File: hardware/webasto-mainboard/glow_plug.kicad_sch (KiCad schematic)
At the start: 23 parts, among them Q11 SSM3J374R, Q12 2N7002, Q13 SUD50P04-08, Q14 SUD50P04-08, Q15 SUD50P04-08, Q16 SUD50P04-08, Q17 SUD50P04-08, Q18 2N7002, Q19 2N7002, U6 LM7805_TO220, U7 INA219BxDCN

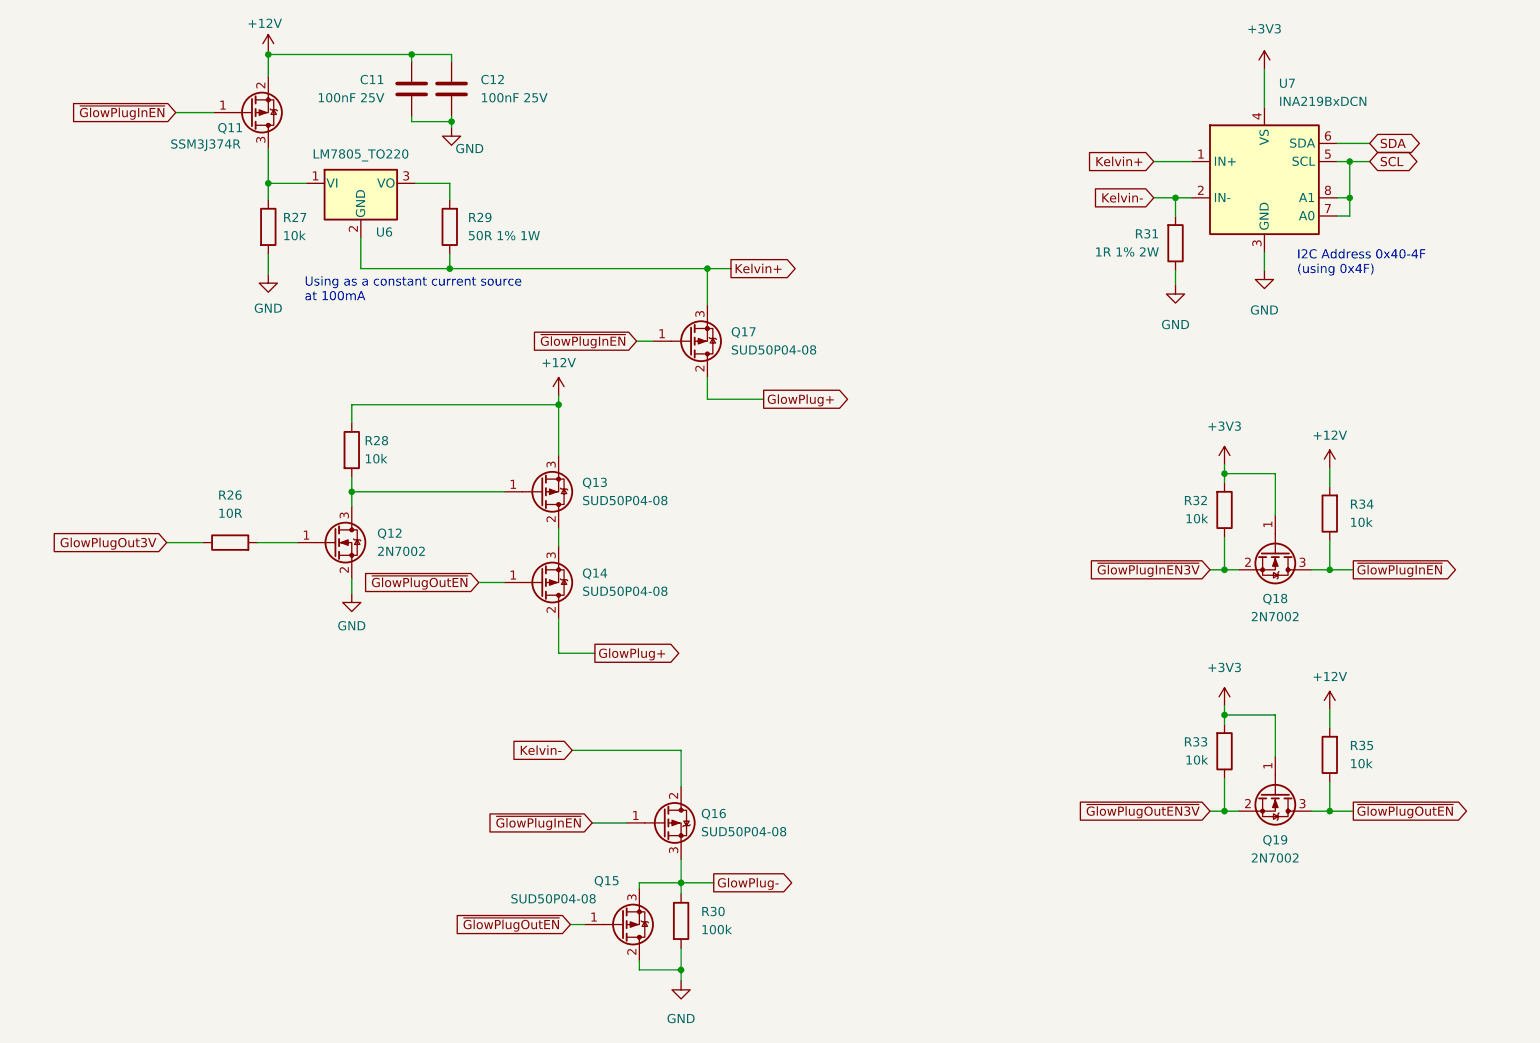
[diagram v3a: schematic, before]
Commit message: Added "USE_USB" input to choose console
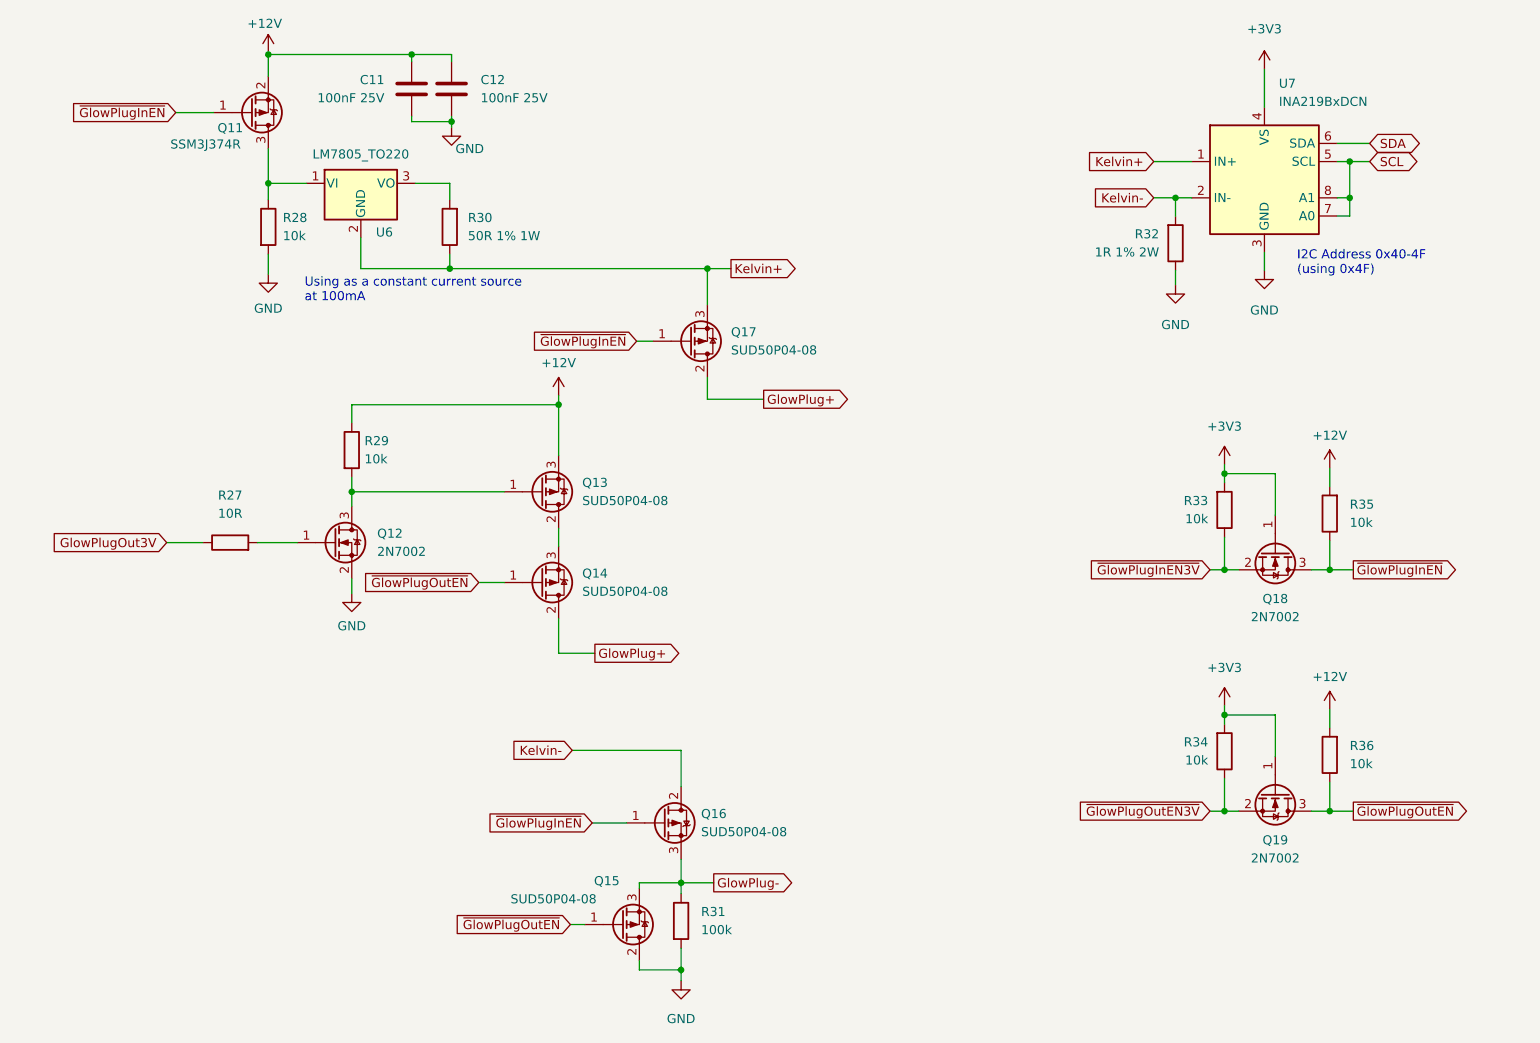
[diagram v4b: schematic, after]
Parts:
- renumbered R26 to R27, R27 to R28, R28 to R29, R29 to R30, R30 to R31, R31 to R32, R32 to R33, R33 to R34, R34 to R35, R35 to R36
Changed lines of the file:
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@@
   (symbol (lib_name "+3V3_1") (lib_id "power:+3V3") (at 202.565 29.972 0) (unit 1)
     (in_bom yes) (on_board yes) (fields_autoplaced)
-    (property "Reference" "#PWR066" (id 0) (at 202.565 33.782 0)
+    (property "Reference" "#PWR068" (id 0) (at 202.565 33.782 0)
       (effects (font (size 1.27 1.27)) hide)
     )
@@
   (symbol (lib_name "GND_8") (lib_id "power:GND") (at 202.565 58.166 0) (unit 1)
     (in_bom yes) (on_board yes) (fields_autoplaced)
-    (property "Reference" "#PWR067" (id 0) (at 202.565 64.516 0)
+    (property "Reference" "#PWR069" (id 0) (at 202.565 64.516 0)
       (effects (font (size 1.27 1.27)) hide)
     )
@@
   (symbol (lib_id "Device:R") (at 120.904 149.225 0) (unit 1)
     (in_bom yes) (on_board yes) (fields_autoplaced)
-    (property "Reference" "R30" (id 0) (at 123.698 147.9549 0)
+    (property "Reference" "R31" (id 0) (at 123.698 147.9549 0)
       (effects (font (size 1.27 1.27)) (justify left))
     )
@@
   (symbol (lib_id "Device:R") (at 74.803 83.312 0) (unit 1)
     (in_bom yes) (on_board yes) (fields_autoplaced)
-    (property "Reference" "R28" (id 0) (at 76.581 82.0419 0)
+    (property "Reference" "R29" (id 0) (at 76.581 82.0419 0)
       (effects (font (size 1.27 1.27)) (justify left))
     )
@@
   (symbol (lib_id "Device:R") (at 88.519 52.07 180) (unit 1)
     (in_bom yes) (on_board yes)
-    (property "Reference" "R29" (id 0) (at 91.059 50.7999 0)
+    (property "Reference" "R30" (id 0) (at 91.059 50.7999 0)
       (effects (font (size 1.27 1.27)) (justify right))
     )
@@
   (symbol (lib_name "+3V3_2") (lib_id "power:+3V3") (at 196.977 85.344 0) (unit 1)
     (in_bom yes) (on_board yes) (fields_autoplaced)
-    (property "Reference" "#PWR064" (id 0) (at 196.977 89.154 0)
+    (property "Reference" "#PWR066" (id 0) (at 196.977 89.154 0)
       (effects (font (size 1.27 1.27)) hide)
     )
@@
   (symbol (lib_name "GND_2") (lib_id "power:GND") (at 74.803 103.378 0) (unit 1)
     (in_bom yes) (on_board yes) (fields_autoplaced)
-    (property "Reference" "#PWR059" (id 0) (at 74.803 109.728 0)
+    (property "Reference" "#PWR061" (id 0) (at 74.803 109.728 0)
       (effects (font (size 1.27 1.27)) hide)
     )
@@
   (symbol (lib_id "Device:R") (at 63.119 52.07 0) (unit 1)
     (in_bom yes) (on_board yes)
-    (property "Reference" "R27" (id 0) (at 65.151 50.7999 0)
+    (property "Reference" "R28" (id 0) (at 65.151 50.7999 0)
       (effects (font (size 1.27 1.27)) (justify left))
     )
@@
   (symbol (lib_name "+3V3_2") (lib_id "power:+3V3") (at 196.977 119.126 0) (unit 1)
     (in_bom yes) (on_board yes) (fields_autoplaced)
-    (property "Reference" "#PWR065" (id 0) (at 196.977 122.936 0)
+    (property "Reference" "#PWR067" (id 0) (at 196.977 122.936 0)
       (effects (font (size 1.27 1.27)) hide)
     )
@@
   (symbol (lib_id "Device:R") (at 57.785 96.266 90) (unit 1)
     (in_bom yes) (on_board yes) (fields_autoplaced)
-    (property "Reference" "R26" (id 0) (at 57.785 89.662 90))
+    (property "Reference" "R27" (id 0) (at 57.785 89.662 90))
     (property "Value" "10R" (id 1) (at 57.785 92.202 90))
     (property "Footprint" "Resistor_SMD:R_0805_2012Metric_Pad1.20x1.40mm_HandSolder" (id 2) (at 57.785 98.044 90)
@@
   (symbol (lib_id "Device:R") (at 196.977 125.476 0) (mirror x) (unit 1)
     (in_bom yes) (on_board yes) (fields_autoplaced)
-    (property "Reference" "R33" (id 0) (at 194.691 124.2059 0)
+    (property "Reference" "R34" (id 0) (at 194.691 124.2059 0)
       (effects (font (size 1.27 1.27)) (justify right))
     )
@@
   (symbol (lib_name "GND_9") (lib_id "power:GND") (at 120.904 157.607 0) (unit 1)
     (in_bom yes) (on_board yes) (fields_autoplaced)
-    (property "Reference" "#PWR062" (id 0) (at 120.904 163.957 0)
+    (property "Reference" "#PWR064" (id 0) (at 120.904 163.957 0)
       (effects (font (size 1.27 1.27)) hide)
     )
@@
   (symbol (lib_name "+12V_3") (lib_id "power:+12V") (at 211.709 85.852 0) (unit 1)
     (in_bom yes) (on_board yes) (fields_autoplaced)
-    (property "Reference" "#PWR068" (id 0) (at 211.709 89.662 0)
+    (property "Reference" "#PWR070" (id 0) (at 211.709 89.662 0)
       (effects (font (size 1.27 1.27)) hide)
     )
@@
   (symbol (lib_name "GND_5") (lib_id "power:GND") (at 88.773 38.1 0) (unit 1)
     (in_bom yes) (on_board yes)
-    (property "Reference" "#PWR060" (id 0) (at 88.773 44.45 0)
+    (property "Reference" "#PWR062" (id 0) (at 88.773 44.45 0)
       (effects (font (size 1.27 1.27)) hide)
     )
@@
   (symbol (lib_id "Device:R") (at 211.709 92.202 180) (unit 1)
     (in_bom yes) (on_board yes) (fields_autoplaced)
-    (property "Reference" "R34" (id 0) (at 214.503 90.9319 0)
+    (property "Reference" "R35" (id 0) (at 214.503 90.9319 0)
       (effects (font (size 1.27 1.27)) (justify right))
     )
@@
   (symbol (lib_name "GND_8") (lib_id "power:GND") (at 190.119 60.198 0) (unit 1)
     (in_bom yes) (on_board yes) (fields_autoplaced)
-    (property "Reference" "#PWR063" (id 0) (at 190.119 66.548 0)
+    (property "Reference" "#PWR065" (id 0) (at 190.119 66.548 0)
       (effects (font (size 1.27 1.27)) hide)
     )
@@
   (symbol (lib_name "+12V_2") (lib_id "power:+12V") (at 63.119 27.686 0) (unit 1)
     (in_bom yes) (on_board yes)
-    (property "Reference" "#PWR057" (id 0) (at 63.119 31.496 0)
+    (property "Reference" "#PWR059" (id 0) (at 63.119 31.496 0)
       (effects (font (size 1.27 1.27)) hide)
     )
@@
   (symbol (lib_name "+12V_3") (lib_id "power:+12V") (at 211.709 119.634 0) (unit 1)
     (in_bom yes) (on_board yes) (fields_autoplaced)
-    (property "Reference" "#PWR069" (id 0) (at 211.709 123.444 0)
+    (property "Reference" "#PWR071" (id 0) (at 211.709 123.444 0)
       (effects (font (size 1.27 1.27)) hide)
     )
@@
   (symbol (lib_name "GND_3") (lib_id "power:GND") (at 63.119 58.674 0) (unit 1)
     (in_bom yes) (on_board yes) (fields_autoplaced)
-    (property "Reference" "#PWR058" (id 0) (at 63.119 65.024 0)
+    (property "Reference" "#PWR060" (id 0) (at 63.119 65.024 0)
       (effects (font (size 1.27 1.27)) hide)
     )
@@
   (symbol (lib_id "Device:R") (at 211.709 125.984 180) (unit 1)
     (in_bom yes) (on_board yes) (fields_autoplaced)
-    (property "Reference" "R35" (id 0) (at 214.503 124.7139 0)
+    (property "Reference" "R36" (id 0) (at 214.503 124.7139 0)
       (effects (font (size 1.27 1.27)) (justify right))
     )
@@
   (symbol (lib_id "Device:R") (at 190.119 54.356 0) (mirror x) (unit 1)
     (in_bom yes) (on_board yes) (fields_autoplaced)
-    (property "Reference" "R31" (id 0) (at 187.833 53.0859 0)
+    (property "Reference" "R32" (id 0) (at 187.833 53.0859 0)
       (effects (font (size 1.27 1.27)) (justify right))
     )
@@
   (symbol (lib_name "+12V_1") (lib_id "power:+12V") (at 103.759 75.692 0) (unit 1)
     (in_bom yes) (on_board yes) (fields_autoplaced)
-    (property "Reference" "#PWR061" (id 0) (at 103.759 79.502 0)
+    (property "Reference" "#PWR063" (id 0) (at 103.759 79.502 0)
       (effects (font (size 1.27 1.27)) hide)
     )
@@
   (symbol (lib_id "Device:R") (at 196.977 91.694 0) (mirror x) (unit 1)
     (in_bom yes) (on_board yes) (fields_autoplaced)
-    (property "Reference" "R32" (id 0) (at 194.691 90.4239 0)
-      (effects (font (size 1.27 1.27)) (justify right))
-    )
+    (property "Reference" "R33" (id 0) (at 194.691 90.4239 0)
+      (effects (font (size 1.27 1.27)) (justify right))
+    )

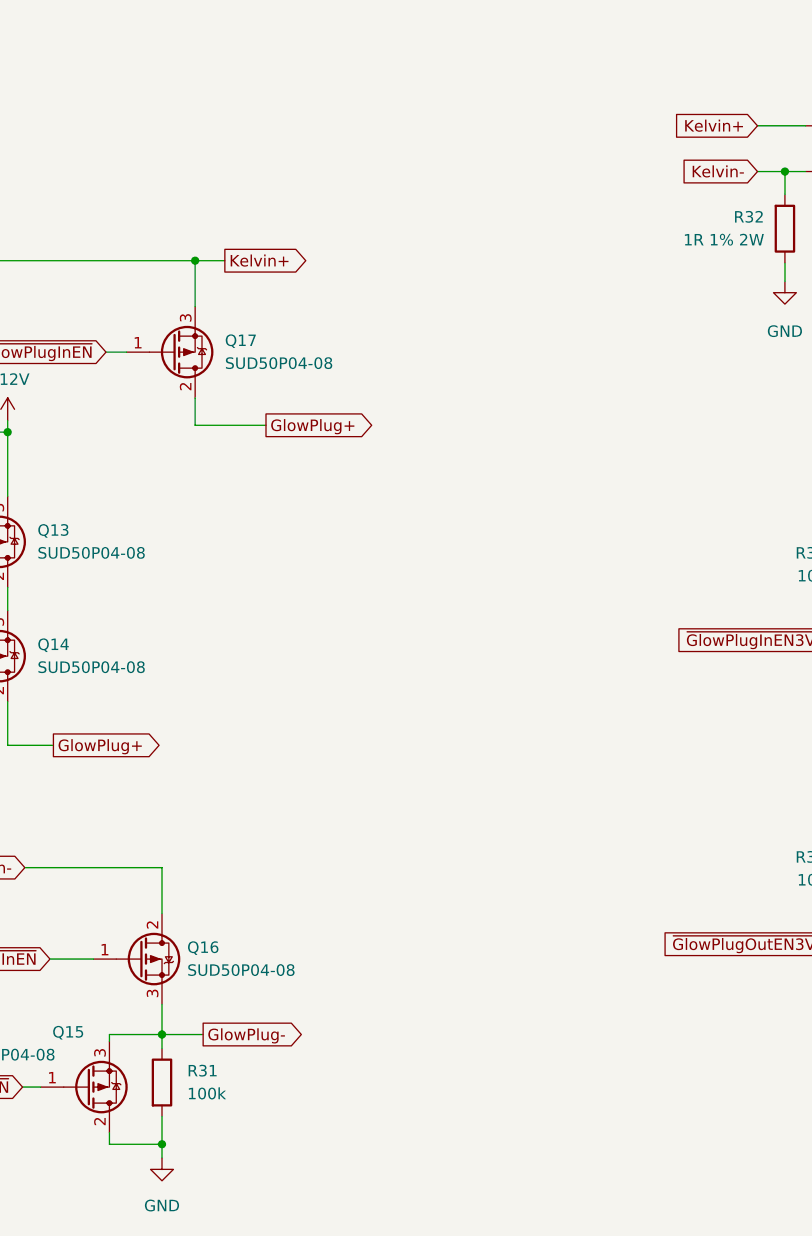
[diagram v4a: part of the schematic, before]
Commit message: Added snubbing diodes on all the inputs
- back EMF from relays... I forgot...  so reverse biased diodes from
  GND to signal and from signal to +12V.
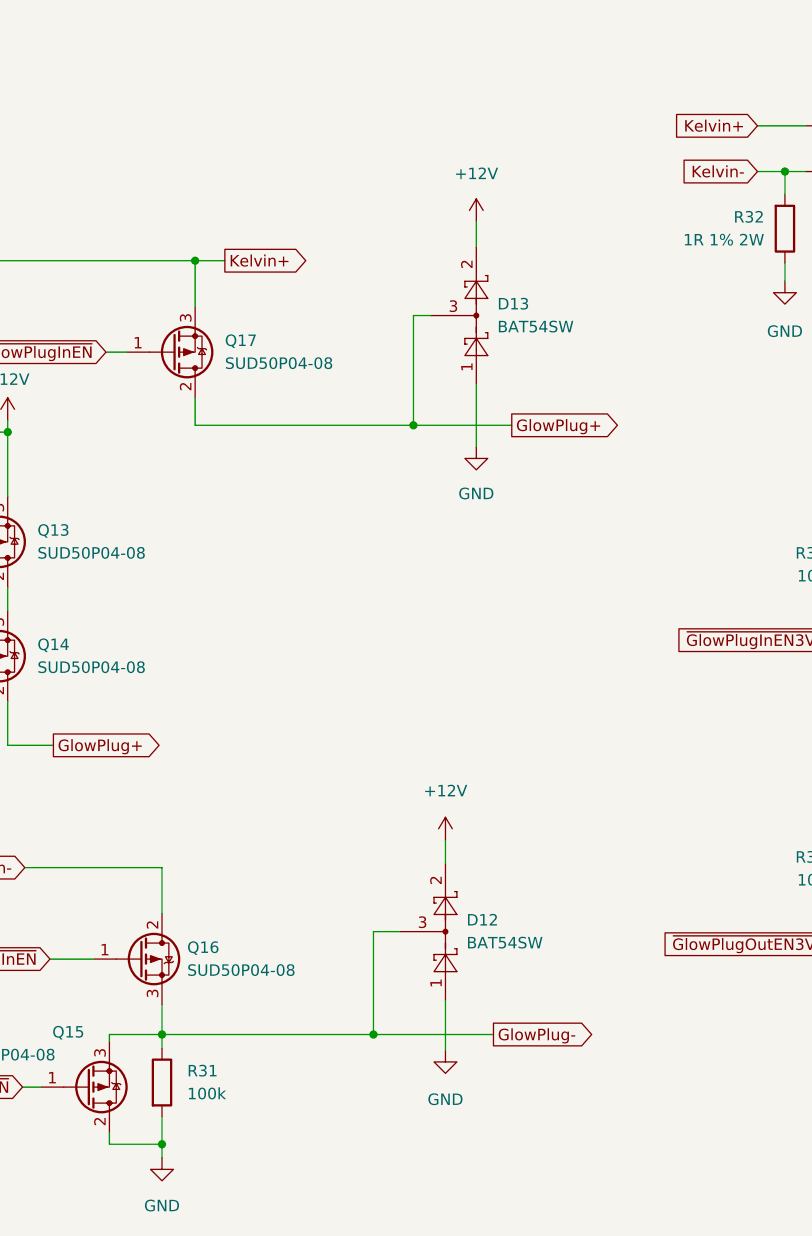
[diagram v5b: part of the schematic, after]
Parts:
- added D12, D13: BAT54SW, Package_TO_SOT_SMD:SOT-323_SC-70, symbol Diode:BAT54SW
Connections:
- net +12V: now also D12.2, D13.2
- net GND: now also D12.1, D13.1
- net GlowPlug+: now also D13.3
- net GlowPlug-: now also D12.3

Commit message: Update title block on mainboard, print PDFs
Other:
- company: (none) -> Gavin Hurlbut
- title: (none) -> Webasto Replacement Mainboard (Thermo Top C)
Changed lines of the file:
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@@
 (kicad_sch (version 20211123) (generator eeschema)
   (paper "A4")
+  (title_block
+    (title "Webasto Replacement Mainboard (Thermo Top C)")
+    (date "2023-01-31")
+    (rev "v1.0")
+    (company "Gavin Hurlbut")
+  )
   (junction (at 144.399 143.891) (diameter 0) (color 0 0 0 0)
   )
